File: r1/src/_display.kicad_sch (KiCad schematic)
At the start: 21 parts, among them J5 AFC07-S24ECA-00, Q6 SSM3K376R, U5 GDEH029A1

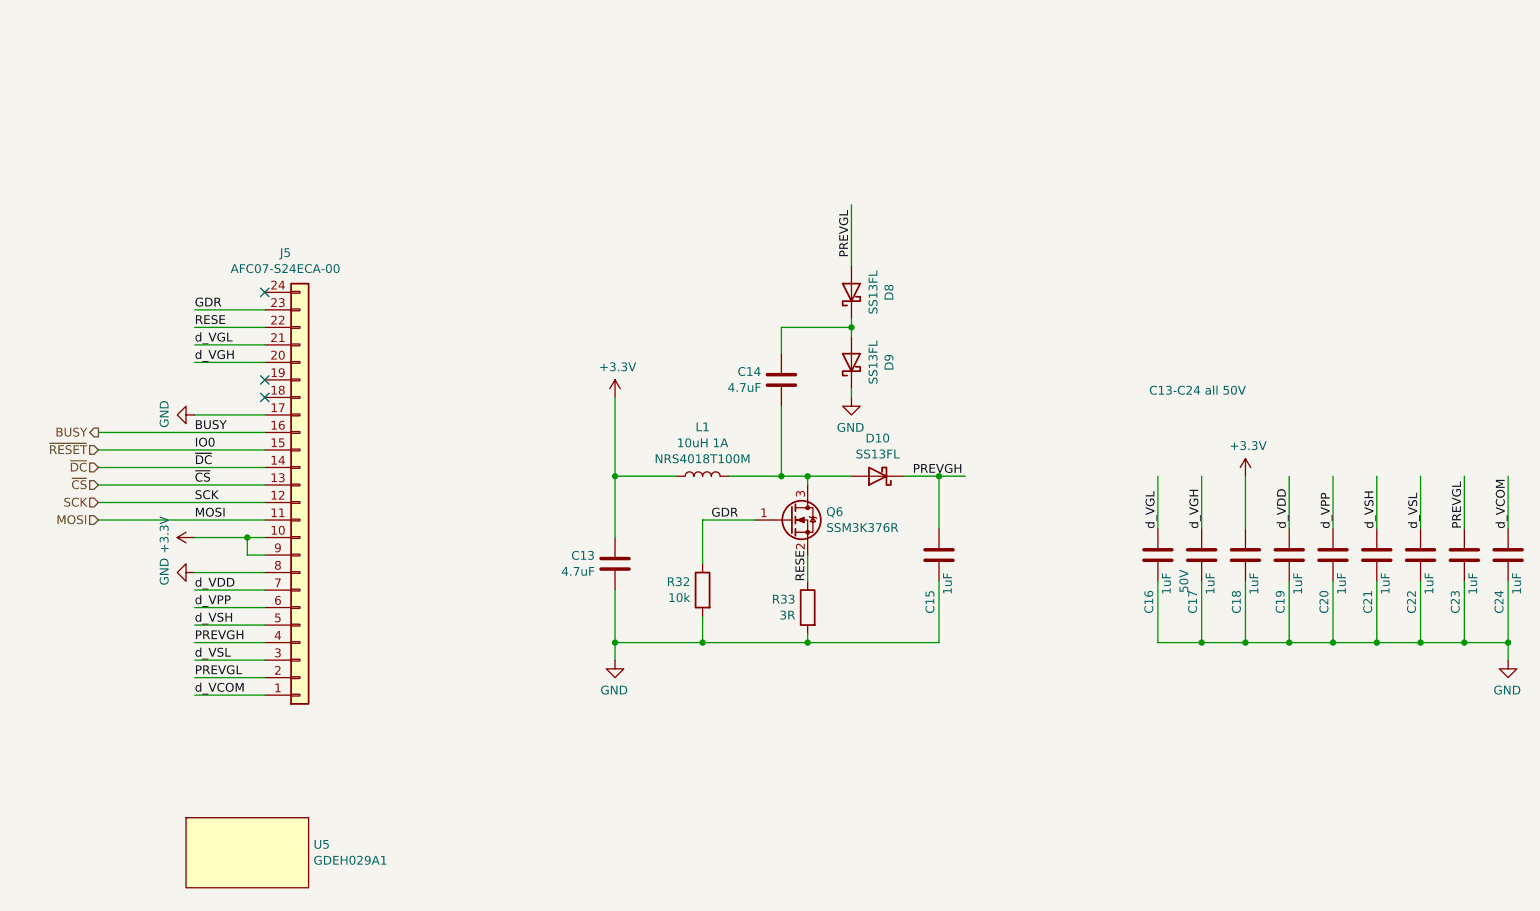
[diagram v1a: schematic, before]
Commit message: Add backlight driver FET, finish display bus wiring
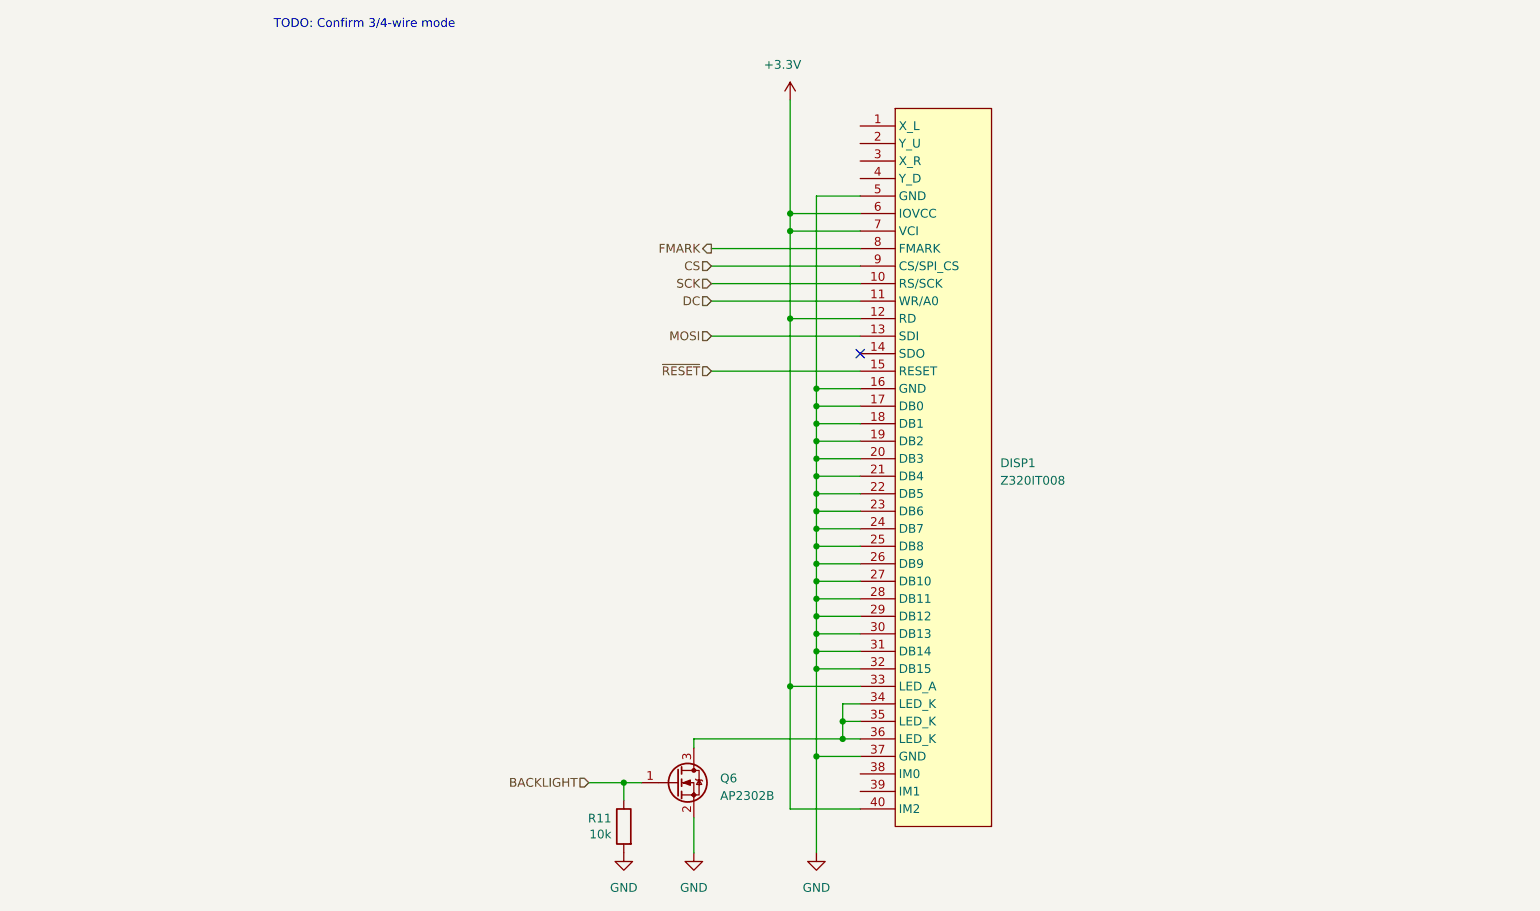
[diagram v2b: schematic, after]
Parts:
- removed C13, C14: 4.7uF, Capacitor_SMD:C_0805_2012Metric, symbol Device:C
- removed C15, C16, C17, C18, C19, C20, C21, C22, C23, C24: 1uF, Capacitor_SMD:C_0603_1608Metric, symbol Device:C
- removed D10, D8, D9: SS13FL, Diode_SMD:D_SOD-123F, symbol Device:D_Schottky
- removed J5: AFC07-S24ECA-00, jeffmakes-footprints:AFC07x24-1MP_P0.5mm_Horizontal, symbol Connector_Generic:Conn_01x24
- removed L1: 10uH 1A, Inductor_SMD:L_Taiyo-Yuden_MD-5050, symbol Device:L
- removed Q6: SSM3K376R, Package_TO_SOT_SMD:SOT-23, symbol Transistor_FET:2N7002
- removed R32: 10k, Resistor_SMD:R_0402_1005Metric, symbol Device:R
- removed R33: 3R, Resistor_SMD:R_0402_1005Metric, symbol Device:R
- removed U5: GDEH029A1, jeffmakes-footprints:GDEH029A1, symbol j_Display:Display_dummy
- added DISP1: Z320IT008, symbol j_Display:Z320IT008
- added Q6: AP2302B, symbol Device:Q_NMOS_GSD
- added R11: 10k, Resistor_SMD:R_0402_1005Metric, symbol Device:R
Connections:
- net +3.3V: now also DISP1.12 (RD), DISP1.33 (LED_A), DISP1.40 (IM2), DISP1.6 (IOVCC), DISP1.7 (VCI)
- net GND: now also DISP1.16 (GND), DISP1.17 (DB0), DISP1.18 (DB1), DISP1.19 (DB2), DISP1.20 (DB3), DISP1.21 (DB4), DISP1.22 (DB5), DISP1.23 (DB6), DISP1.24 (DB7), DISP1.25 (DB8), DISP1.26 (DB9), DISP1.27 (DB10), DISP1.28 (DB11), DISP1.29 (DB12), DISP1.30 (DB13), DISP1.31 (DB14), DISP1.32 (DB15), DISP1.37 (GND), DISP1.5 (GND), Q6.2 (S), R11.2
- net MOSI: now also DISP1.13 (SDI)
- net SCK: now also DISP1.10 (RS/SCK)
- net ~{RESET}: now also DISP1.15 (RESET)
- new net: DISP1.34 (LED_K), DISP1.35 (LED_K), DISP1.36 (LED_K), Q6.3 (D)
- new net BACKLIGHT: Q6.1 (G), R11.1
- new net CS: DISP1.9 (CS/SPI_CS)
- new net DC: DISP1.11 (WR/A0)
- new net FMARK: DISP1.8 (FMARK)
- no-connect marks 3 -> 1
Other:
- note added: "TODO: Confirm 3/4-wire mode"
- note removed: "C13-C24 all 50V"

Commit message: add TODO
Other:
- note added: "TODO: Confirm touch"
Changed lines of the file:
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@@
+    (effects (font (size 1.27 1.27)) (justify left bottom))
+  )
+  (text "TODO: Confirm touch" (at 68.58 39.37 0)
     (effects (font (size 1.27 1.27)) (justify left bottom))
   )

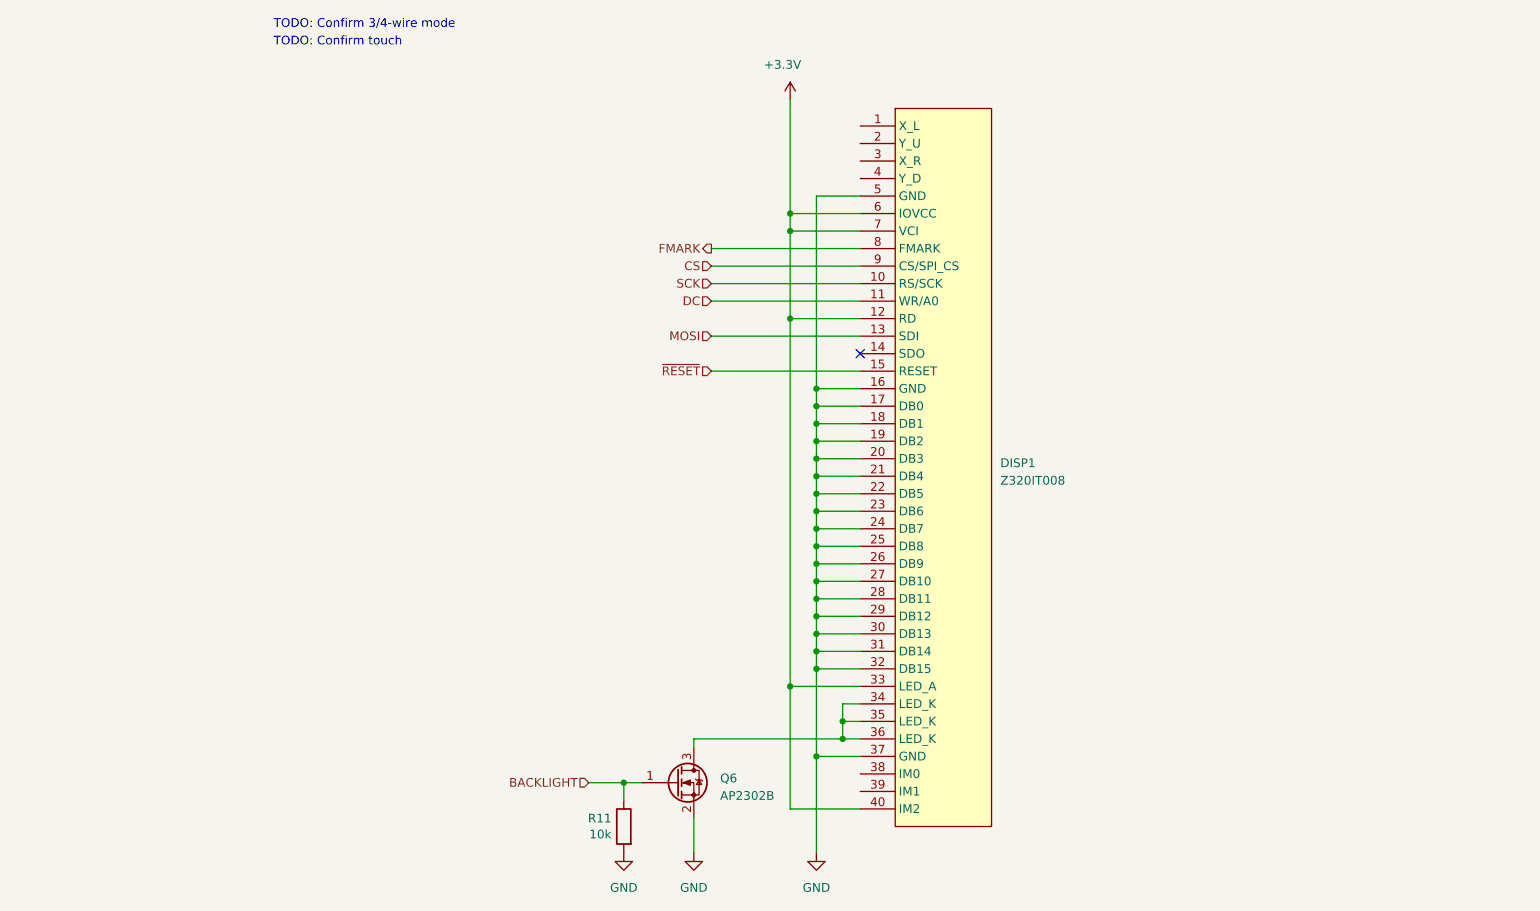
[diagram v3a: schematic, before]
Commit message: Replace display symbol with FFC connector, otherwise we won't have separate BOM entries for the display and connector
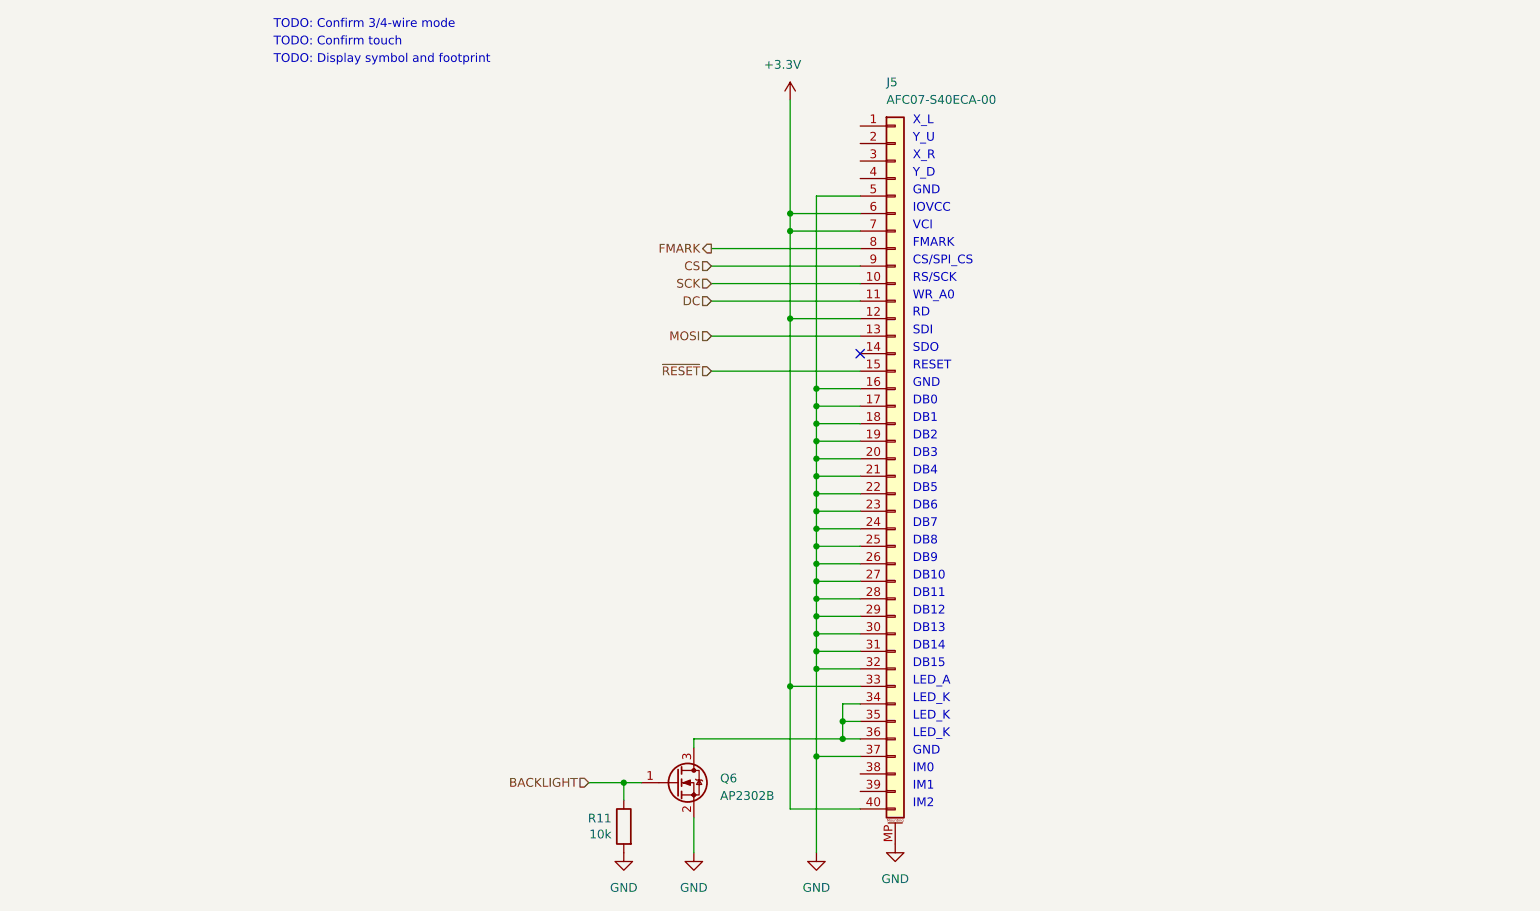
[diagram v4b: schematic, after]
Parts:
- removed DISP1: Z320IT008, symbol j_Display:Z320IT008
- added J5: AFC07-S40ECA-00, symbol Connector_Generic_MountingPin:Conn_01x40_MountingPin
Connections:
- net +3.3V: now also J5.12 (Pin_12), J5.33 (Pin_33), J5.40 (Pin_40), J5.6 (Pin_6), J5.7 (Pin_7)
- net CS: now also J5.9 (Pin_9)
- net DC: now also J5.11 (Pin_11)
- net FMARK: now also J5.8 (Pin_8)
- net GND: now also J5.16 (Pin_16), J5.17 (Pin_17), J5.18 (Pin_18), J5.19 (Pin_19), J5.20 (Pin_20), J5.21 (Pin_21), J5.22 (Pin_22), J5.23 (Pin_23), J5.24 (Pin_24), J5.25 (Pin_25), J5.26 (Pin_26), J5.27 (Pin_27), J5.28 (Pin_28), J5.29 (Pin_29), J5.30 (Pin_30), J5.31 (Pin_31), J5.32 (Pin_32), J5.37 (Pin_37), J5.5 (Pin_5), J5.MP (MountPin)
- net MOSI: now also J5.13 (Pin_13)
- net SCK: now also J5.10 (Pin_10)
- net ~{RESET}: now also J5.15 (Pin_15)
- net at Q6.3 (D): now also J5.34 (Pin_34), J5.35 (Pin_35), J5.36 (Pin_36)
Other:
- note added: "CS/SPI_CS"
- note added: "DB0"
- note added: "DB1"
- note added: "DB10"
- note added: "DB11"
- note added: "DB12"
- note added: "DB13"
- note added: "DB14"
- note added: "DB15"
- note added: "DB2"
- note added: "DB3"
- note added: "DB4"
- note added: "DB5"
- note added: "DB6"
- note added: "DB7"
- note added: "DB8"
- note added: "DB9"
- note added: "FMARK"
- note added: "GND"
- note added: "IM0"
- note added: "IM1"
- note added: "IM2"
- note added: "IOVCC"
- note added: "LED_A"
- note added: "LED_K"
- note added: "RD"
- note added: "RESET"
- note added: "RS/SCK"
- note added: "SDI"
- note added: "SDO"
- note added: "TODO: Display symbol and footprint"
- note added: "VCI"
- note added: "WR_A0"
- note added: "X_L"
- note added: "X_R"
- note added: "Y_D"
- note added: "Y_U"
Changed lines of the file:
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@@
     (stroke (width 0) (type default))
   )
+  (text "GND" (at 161.29 60.96 0)
+    (effects (font (size 1.27 1.27)) (justify left bottom))
+  )
+  (text "RESET" (at 161.29 86.36 0)
+    (effects (font (size 1.27 1.27)) (justify left bottom))
+  )
+  (text "LED_A" (at 161.29 132.08 0)
+    (effects (font (size 1.27 1.27)) (justify left bottom))
+  )
+  (text "X_R" (at 161.29 55.88 0)
+    (effects (font (size 1.27 1.27)) (justify left bottom))
+  )
+  (text "DB12" (at 161.29 121.92 0)
+    (effects (font (size 1.27 1.27)) (justify left bottom))
+  )
+  (text "IM1" (at 161.29 147.32 0)
+    (effects (font (size 1.27 1.27)) (justify left bottom))
+  )
+  (text "SDO" (at 161.29 83.82 0)
+    (effects (font (size 1.27 1.27)) (justify left bottom))
+  )
+  (text "DB2" (at 161.29 96.52 0)
+    (effects (font (size 1.27 1.27)) (justify left bottom))
+  )
+  (text "IM0" (at 161.29 144.78 0)
+    (effects (font (size 1.27 1.27)) (justify left bottom))
+  )
+  (text "DB14" (at 161.29 127 0)
+    (effects (font (size 1.27 1.27)) (justify left bottom))
+  )
+  (text "DB5" (at 161.29 104.14 0)
+    (effects (font (size 1.27 1.27)) (justify left bottom))
+  )
+  (text "GND" (at 161.29 142.24 0)
+    (effects (font (size 1.27 1.27)) (justify left bottom))
+  )
+  (text "DB7" (at 161.29 109.22 0)
+    (effects (font (size 1.27 1.27)) (justify left bottom))
+  )
+  (text "DB6" (at 161.29 106.68 0)
+    (effects (font (size 1.27 1.27)) (justify left bottom))
+  )
   (text "TODO: Confirm 3/4-wire mode" (at 68.58 36.83 0)
     (effects (font (size 1.27 1.27)) (justify left bottom))
   )
+  (text "DB1" (at 161.29 93.98 0)
+    (effects (font (size 1.27 1.27)) (justify left bottom))
+  )
+  (text "LED_K" (at 161.29 139.7 0)
+    (effects (font (size 1.27 1.27)) (justify left bottom))
+  )
+  (text "DB11" (at 161.29 119.38 0)
+    (effects (font (size 1.27 1.27)) (justify left bottom))
+  )
+  (text "SDI" (at 161.29 81.28 0)
+    (effects (font (size 1.27 1.27)) (justify left bottom))
+  )
+  (text "GND" (at 161.29 88.9 0)
+    (effects (font (size 1.27 1.27)) (justify left bottom))
+  )
+  (text "DB15" (at 161.29 129.54 0)
+    (effects (font (size 1.27 1.27)) (justify left bottom))
+  )
+  (text "DB8" (at 161.29 111.76 0)
+    (effects (font (size 1.27 1.27)) (justify left bottom))
+  )
+  (text "TODO: Display symbol and footprint" (at 68.58 41.91 0)
+    (effects (font (size 1.27 1.27)) (justify left bottom))
+  )
+  (text "RD" (at 161.2511 78.6778 0)
+    (effects (font (size 1.27 1.27)) (justify left bottom))
+  )
+  (text "DB3" (at 161.29 99.06 0)
+    (effects (font (size 1.27 1.27)) (justify left bottom))
+  )
+  (text "DB9" (at 161.29 114.3 0)
+    (effects (font (size 1.27 1.27)) (justify left bottom))
+  )
   (text "TODO: Confirm touch" (at 68.58 39.37 0)
+    (effects (font (size 1.27 1.27)) (justify left bottom))
+  )
+  (text "DB0" (at 161.29 91.44 0)
+    (effects (font (size 1.27 1.27)) (justify left bottom))
+  )
+  (text "IOVCC" (at 161.29 63.5 0)
+    (effects (font (size 1.27 1.27)) (justify left bottom))
+  )
+  (text "CS/SPI_CS" (at 161.29 71.12 0)
+    (effects (font (size 1.27 1.27)) (justify left bottom))
+  )
+  (text "VCI" (at 161.29 66.04 0)
+    (effects (font (size 1.27 1.27)) (justify left bottom))
+  )
+  (text "DB10" (at 161.29 116.84 0)
+    (effects (font (size 1.27 1.27)) (justify left bottom))
+  )
+  (text "FMARK" (at 161.29 68.58 0)
+    (effects (font (size 1.27 1.27)) (justify left bottom))
+  )
+  (text "Y_U" (at 161.29 53.34 0)
+    (effects (font (size 1.27 1.27)) (justify left bottom))
+  )
+  (text "WR_A0" (at 161.29 76.2 0)
+    (effects (font (size 1.27 1.27)) (justify left bottom))
+  )
+  (text "RS/SCK" (at 161.29 73.66 0)
+    (effects (font (size 1.27 1.27)) (justify left bottom))
+  )
+  (text "DB4" (at 161.29 101.6 0)
+    (effects (font (size 1.27 1.27)) (justify left bottom))
+  )
+  (text "IM2" (at 161.29 149.86 0)
+    (effects (font (size 1.27 1.27)) (justify left bottom))
+  )
+  (text "LED_K" (at 161.29 137.16 0)
+    (effects (font (size 1.27 1.27)) (justify left bottom))
+  )
+  (text "Y_D" (at 161.29 58.42 0)
+    (effects (font (size 1.27 1.27)) (justify left bottom))
+  )
+  (text "X_L" (at 161.29 50.8 0)
+    (effects (font (size 1.27 1.27)) (justify left bottom))
+  )
+  (text "LED_K" (at 161.29 134.62 0)
+    (effects (font (size 1.27 1.27)) (justify left bottom))
+  )
+  (text "DB13" (at 161.29 124.46 0)
     (effects (font (size 1.27 1.27)) (justify left bottom))
   )
@@
     )
   )
-  (symbol (lib_id "j_Display:Z320IT008") (at 165.1 100.33 0) (unit 1)
-    (in_bom yes) (on_board yes) (dnp no) (fields_autoplaced)
-    (property "Reference" "DISP1" (at 173.99 99.695 0)
-      (effects (font (size 1.27 1.27)) (justify left))
-    )
-    (property "Value" "Z320IT008" (at 173.99 102.235 0)
-      (effects (font (size 1.27 1.27)) (justify left))
-    )
-    (property "Footprint" "" (at 167.64 72.39 0)
-      (effects (font (size 1.27 1.27)) hide)
-    )
-    (property "Datasheet" "" (at 167.64 72.39 0)
+  (symbol (lib_id "Connector_Generic_MountingPin:Conn_01x40_MountingPin") (at 158.75 99.06 0) (unit 1)
+    (in_bom yes) (on_board yes) (dnp no)
+    (property "Reference" "J5" (at 157.48 44.45 0)
+      (effects (font (size 1.27 1.27)) (justify left))
+    )
+    (property "Value" "AFC07-S40ECA-00" (at 157.48 46.99 0)
+      (effects (font (size 1.27 1.27)) (justify left))
+    )
+    (property "Footprint" "" (at 158.75 99.06 0)
+      (effects (font (size 1.27 1.27)) hide)
+    )
+    (property "Datasheet" "~" (at 158.75 99.06 0)
+      (effects (font (size 1.27 1.27)) hide)
+    )
+    (property "MPN" "AFC07-S40ECA-00" (at 158.75 99.06 0)
+      (effects (font (size 1.27 1.27)) hide)
+    )
+    (property "LCSC" "C262648" (at 158.75 99.06 0)
       (effects (font (size 1.27 1.27)) hide)
     )
@@
     (pin "8")
     (pin "9")
-    (instances
-      (project "tr23-badge-r1"
-        (path "/ab725fe7-4504-40ef-b6af-82d065d00fb6/00000000-0000-0000-0000-00005e536877"
-          (reference "DISP1") (unit 1)
-        )
-      )
+    (pin "MP")
+    (instances
+      (project "tr23-badge-r1"
+        (path "/ab725fe7-4504-40ef-b6af-82d065d00fb6/00000000-0000-0000-0000-00005e536877"
+          (reference "J5") (unit 1)
+        )
+      )
+    )
+  )
+  (symbol (lib_id "power:GND") (at 158.75 154.94 0) (unit 1)
+    (in_bom yes) (on_board yes) (dnp no) (fields_autoplaced)
+    (property "Reference" "#PWR058" (at 158.75 161.29 0)
+      (effects (font (size 1.27 1.27)) hide)
+    )
+    (property "Value" "GND" (at 158.75 160.02 0)
+      (effects (font (size 1.27 1.27)))
+    )
+    (property "Footprint" "" (at 158.75 154.94 0)
+      (effects (font (size 1.27 1.27)) hide)
+    )
+    (property "Datasheet" "" (at 158.75 154.94 0)
+      (effects (font (size 1.27 1.27)) hide)
+    )
+    (pin "1")
+    (instances
+      (project "tr23-badge-r1"
+        (path "/ab725fe7-4504-40ef-b6af-82d065d00fb6/00000000-0000-0000-0000-00005e536877"
+          (reference "#PWR058") (unit 1)
+        )
+      )

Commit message: Assign MPN's and LCSC part numbers
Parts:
- Q6: LCSC (none) -> C5224180; MPN (none) -> AP2302B
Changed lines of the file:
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@@
+      (effects (font (size 1.27 1.27)) hide)
+    )
+    (property "MPN" "AP2302B" (at 127 146.05 0)
+      (effects (font (size 1.27 1.27)) hide)
+    )
+    (property "LCSC" "C5224180" (at 127 146.05 0)
       (effects (font (size 1.27 1.27)) hide)
     )

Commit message: Assign manufacturers
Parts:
- J5: Manufacturer (none) -> Jushuo
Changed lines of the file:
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@@
+      (effects (font (size 1.27 1.27)) hide)
+    )
+    (property "Manufacturer" "Jushuo" (at 158.75 99.06 0)
       (effects (font (size 1.27 1.27)) hide)
     )
